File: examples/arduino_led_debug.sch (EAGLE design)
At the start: 3 parts

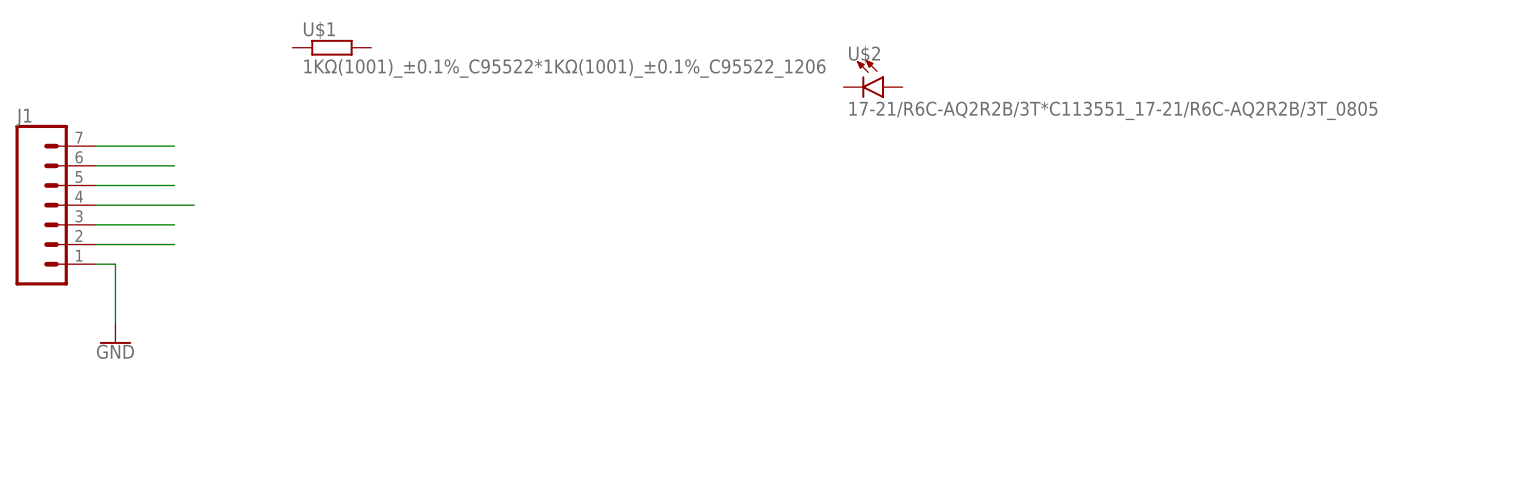
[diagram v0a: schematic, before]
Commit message: Improving library. Still no real LED library! Added example project to test ULPs against.
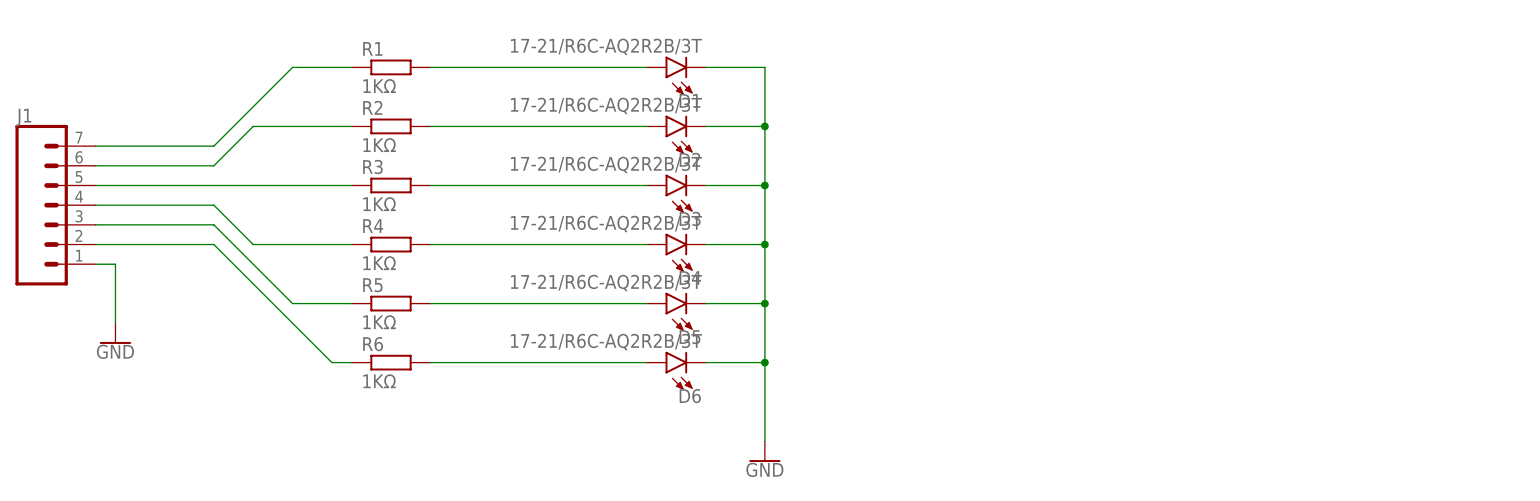
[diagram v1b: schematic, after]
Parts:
- removed U$1: 1KΩ(1001)_±0.1%_C95522*1KΩ(1001)_±0.1%_C95522_1206, Resistors:1KΩ(1001)_±0.1%_C95522*1KΩ(1001)_±0.1%_C95522_1206
- removed U$2: 17-21/R6C-AQ2R2B/3T*C113551_17-21/R6C-AQ2R2B/3T_0805, Optocouplers & LEDs & Infrared:17-21/R6C-AQ2R2B/3T*C113551_17-21/R6C-AQ2R2B/3T_0805
- added D1, D2, D3, D4, D5, D6: 17-21/R6C-AQ2R2B/3T, Optocouplers & LEDs & Infrared.expanded:1721R6CAQ2R2B3TX_C113551_1721R6CAQ2R2B3T_0805
- added R1, R2, R3, R4, R5, R6: 1KΩ, Resistors.basic:1K_1001_1%_C11702_1K_1001_1%_0402
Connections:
- new net N$1: D1.A, R1.2
- new net N$11: D5.A, R5.2
- new net N$12: D6.A, R6.2
- new net N$2: D2.A, R2.2
- new net N$3: D3.A, R3.2
- new net N$5: D4.A, R4.2
- net GND: now also D1.C, D2.C, D3.C, D4.C, D5.C, D6.C
- net N$10: now also R2.1
- net N$4: now also R1.1
- net N$6: now also R6.1
- net N$7: now also R5.1
- net N$8: now also R4.1
- net N$9: now also R3.1
